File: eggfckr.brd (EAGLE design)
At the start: 100 x 80 mm, 7 parts, among them IC1 LM555N

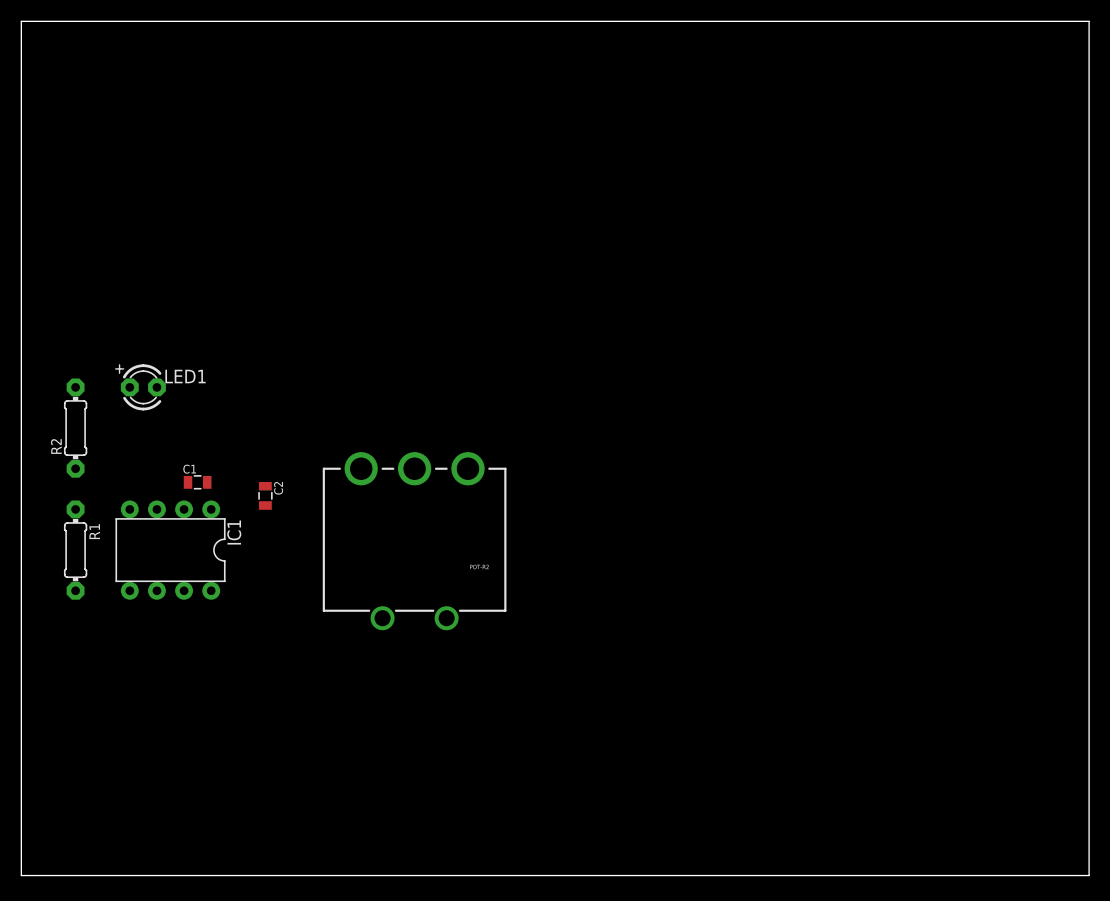
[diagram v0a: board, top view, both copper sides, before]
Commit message: attiny85 version
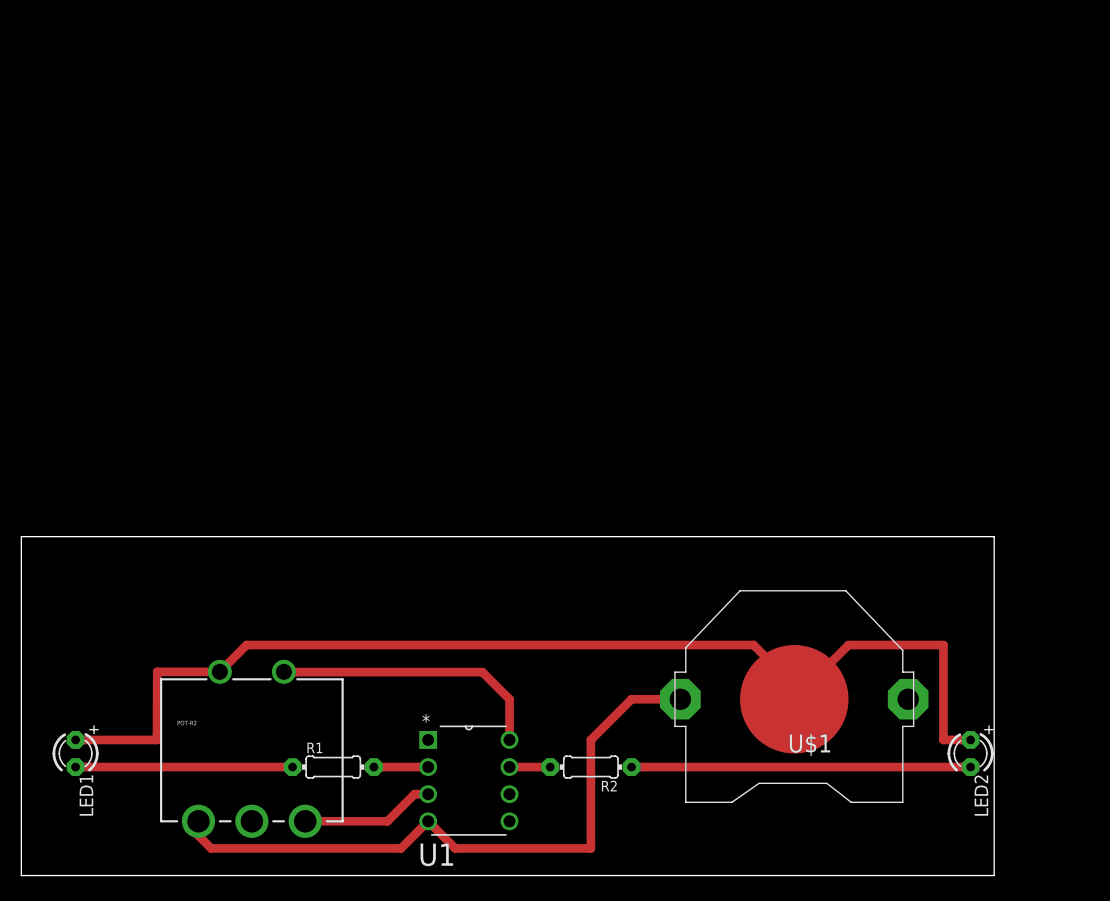
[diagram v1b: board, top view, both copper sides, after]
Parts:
- removed C1: 47uF, ATtami:0805
- removed C2: 10nF, ATtami:0805
- removed IC1: LM555N, adafruit:DIL08-ROUND
- added LED2: (no value), adafruit:LED3MM
- added U$1: (no value), adafruit:CR2032-THRU
- added U1: ATTINY85-20PU, Atmel_By_element14_Batch_1-00:DIP254P762X533-8
- moved R2 57.8 mm to (53.3, 10.2), turned to 180 degrees
- moved POT-R2 36.4 mm to (21.6, 5.08), turned to 0 degrees
- moved LED1 34.9 mm to (5.08, 11.4), turned to 270 degrees
- moved R1 31.5 mm to (29.2, 10.2), turned to 0 degrees
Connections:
- removed net N$5: IC1.8, POT-R2.S2
- removed net OUTPUT: IC1.3, LED1.K
- new net N$7: LED2.K, R2.1
- net GND: now also POT-R2.E@1, U$1.+2, U1.4; no longer C1.2, C2.1, IC1.1
- net N$1: now also R2.2, U1.7; no longer C2.2, IC1.5
- net N$2: now also POT-R2.E@2, U1.3; no longer C1.1, IC1.2, IC1.6, POT-R2.E@1
- net N$3: now also POT-R2.S2, U1.8; no longer POT-R2.S1
- net N$4: now also U1.2; no longer IC1.7, POT-R2.E@2
- net N$6: now also LED1.K, R1.1; no longer LED1.A, R2.2
- net VCC: now also LED1.A, LED2.A, POT-R2.S1, U$1.-; no longer IC1.4, R1.1, R2.1
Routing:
- net VCC: track 0.00 -> 108.1 mm
- net GND: track 0.00 -> 60.8 mm
- net N$7: track 0.00 -> 31.8 mm
- net N$3: track 0.00 -> 26.0 mm
- net N$6: track 0.00 -> 20.3 mm
- net N$2: track 0.00 -> 12.6 mm
- net N$4: track 0.00 -> 5.08 mm
- net N$1: track 0.00 -> 3.81 mm
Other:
- board size 100 x 80 mm -> 91.1 x 31.7 mm
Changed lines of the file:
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@@
 <board>
 <plain>
-<wire x1="0" y1="0" x2="100" y2="0" width="0" layer="20"/>
-<wire x1="100" y1="0" x2="100" y2="80" width="0" layer="20"/>
-<wire x1="100" y1="80" x2="0" y2="80" width="0" layer="20"/>
-<wire x1="0" y1="80" x2="0" y2="0" width="0" layer="20"/>
+<wire x1="0" y1="0" x2="91.11" y2="0" width="0" layer="20"/>
+<wire x1="91.11" y1="0" x2="91.11" y2="31.74" width="0" layer="20"/>
+<wire x1="91.11" y1="31.74" x2="0" y2="31.74" width="0" layer="20"/>
+<wire x1="0" y1="31.74" x2="0" y2="0" width="0" layer="20"/>
 </plain>
 <attributes>
@@
 </autorouter>
 <elements>
-<element name="C1" library="ATtami" package="0805" value="47uF" x="16.51" y="36.83"/>
-<element name="C2" library="ATtami" package="0805" value="10nF" x="22.86" y="35.56" rot="R270"/>
-<element name="IC1" library="adafruit" package="DIL08-ROUND" value="LM555N" x="13.97" y="30.48" rot="R180"/>
-<element name="POT-R2" library="SparkFun-Electromechanical" package="POT_PTH" value="5K" x="36.83" y="38.1" rot="R180"/>
-<element name="R1" library="adafruit" package="0204/7" value="" x="5.08" y="30.48" rot="R270"/>
-<element name="LED1" library="adafruit" package="LED3MM" value="" x="11.43" y="45.72"/>
-<element name="R2" library="adafruit" package="0204/7" value="" x="5.08" y="41.91" rot="R90"/>
+<element name="POT-R2" library="SparkFun-Electromechanical" package="POT_PTH" value="5K" x="21.59" y="5.08"/>
+<element name="LED1" library="adafruit" package="LED3MM" value="" x="5.08" y="11.43" rot="R270"/>
+<element name="R2" library="adafruit" package="0204/7" value="" x="53.34" y="10.16" rot="R180"/>
+<element name="U1" library="Atmel_By_element14_Batch_1-00" package="DIP254P762X533-8" value="ATTINY85-20PU" x="45.72" y="5.08">
+<attribute name="PACKAGE" value="PDIP-8" x="45.72" y="5.08" size="1.778" layer="27" display="off"/>
+<attribute name="OC_NEWARK" value="58M3796" x="45.72" y="5.08" size="1.778" layer="27" display="off"/>
+<attribute name="MPN" value="ATTINY85-20PU" x="45.72" y="5.08" size="1.778" layer="27" display="off"/>
+<attribute name="SUPPLIER" value="Atmel" x="45.72" y="5.08" size="1.778" layer="27" display="off"/>
+<attribute name="OC_FARNELL" value="1455162" x="45.72" y="5.08" size="1.778" layer="27" display="off"/>
+</element>
+<element name="R1" library="adafruit" package="0204/7" value="" x="29.21" y="10.16"/>
+<element name="LED2" library="adafruit" package="LED3MM" value="" x="88.9" y="11.43" rot="R270"/>
+<element name="U$1" library="adafruit" package="CR2032-THRU" value="" x="72.39" y="16.51" rot="R180"/>
 </elements>
 <signals>
 <signal name="N$1">
-<contactref element="C2" pad="2"/>
-<contactref element="IC1" pad="5"/>
-<wire x1="10.16" y1="26.67" x2="22.86" y2="34.66" width="0" layer="19" extent="1-1"/>
+<contactref element="U1" pad="7"/>
+<contactref element="R2" pad="2"/>
+<wire x1="45.72" y1="10.16" x2="49.53" y2="10.16" width="0.8128" layer="1"/>
+</signal>
+<signal name="N$6">
+<contactref element="R1" pad="1"/>
+<contactref element="LED1" pad="K"/>
+<wire x1="5.08" y1="10.16" x2="25.4" y2="10.16" width="0.8128" layer="1"/>
+</signal>
+<signal name="N$7">
+<contactref element="R2" pad="1"/>
+<contactref element="LED2" pad="K"/>
+<wire x1="57.15" y1="10.16" x2="88.9" y2="10.16" width="0.8128" layer="1"/>
 </signal>
 <signal name="GND">
-<contactref element="C2" pad="1"/>
-<contactref element="IC1" pad="1"/>
-<contactref element="C1" pad="2"/>
-<wire x1="17.41" y1="36.83" x2="22.86" y2="36.46" width="0" layer="19" extent="1-1"/>
-<wire x1="17.78" y1="34.29" x2="17.41" y2="36.83" width="0" layer="19" extent="1-1"/>
+<contactref element="U1" pad="4"/>
+<contactref element="POT-R2" pad="E@1"/>
+<contactref element="U$1" pad="+2"/>
+<wire x1="16.59" y1="5.08" x2="16.59" y2="3.73" width="0.8128" layer="1"/>
+<wire x1="16.59" y1="3.73" x2="17.78" y2="2.54" width="0.8128" layer="1"/>
+<wire x1="17.78" y1="2.54" x2="35.56" y2="2.54" width="0.8128" layer="1"/>
+<wire x1="35.56" y1="2.54" x2="38.1" y2="5.08" width="0.8128" layer="1"/>
+<wire x1="61.722" y1="16.51" x2="57.15" y2="16.51" width="0.8128" layer="1"/>
+<wire x1="57.15" y1="16.51" x2="53.34" y2="12.7" width="0.8128" layer="1"/>
+<wire x1="53.34" y1="12.7" x2="53.34" y2="2.54" width="0.8128" layer="1"/>
+<wire x1="53.34" y1="2.54" x2="40.64" y2="2.54" width="0.8128" layer="1"/>
+<wire x1="40.64" y1="2.54" x2="38.1" y2="5.08" width="0.8128" layer="1"/>
 </signal>
 <signal name="VCC">
-<contactref element="R1" pad="1"/>
-<contactref element="IC1" pad="4"/>
-<contactref element="R2" pad="1"/>
-<wire x1="5.08" y1="34.29" x2="10.16" y2="34.29" width="0" layer="19" extent="1-1"/>
-<wire x1="5.08" y1="38.1" x2="5.08" y2="34.29" width="0" layer="19" extent="1-1"/>
+<contactref element="POT-R2" pad="S1"/>
+<contactref element="LED2" pad="A"/>
+<contactref element="LED1" pad="A"/>
+<contactref element="U$1" pad="-"/>
+<wire x1="88.9" y1="12.7" x2="86.36" y2="12.7" width="0.8128" layer="1"/>
+<wire x1="86.36" y1="12.7" x2="86.36" y2="21.59" width="0.8128" layer="1"/>
+<wire x1="86.36" y1="21.59" x2="77.47" y2="21.59" width="0.8128" layer="1"/>
+<wire x1="77.47" y1="21.59" x2="72.39" y2="16.51" width="0.8128" layer="1"/>
+<wire x1="72.39" y1="16.51" x2="71.12" y2="15.24" width="0.8128" layer="1"/>
+<wire x1="71.12" y1="15.24" x2="71.12" y2="16.51" width="0.8128" layer="1"/>
+<wire x1="72.39" y1="16.51" x2="72.39" y2="17.78" width="0.8128" layer="1"/>
+<wire x1="72.39" y1="17.78" x2="68.58" y2="21.59" width="0.8128" layer="1"/>
+<wire x1="68.58" y1="21.59" x2="21.1" y2="21.59" width="0.8128" layer="1"/>
+<wire x1="21.1" y1="21.59" x2="18.59" y2="19.08" width="0.8128" layer="1"/>
+<wire x1="18.59" y1="19.08" x2="12.73" y2="19.08" width="0.8128" layer="1"/>
+<wire x1="12.73" y1="19.08" x2="12.7" y2="12.7" width="0.8128" layer="1"/>
+<wire x1="12.7" y1="12.7" x2="5.08" y2="12.7" width="0.8128" layer="1"/>
+</signal>
+<signal name="N$3">
+<contactref element="U1" pad="8"/>
+<contactref element="POT-R2" pad="S2"/>
+<wire x1="45.72" y1="12.7" x2="45.72" y2="16.51" width="0.8128" layer="1"/>
+<wire x1="45.72" y1="16.51" x2="43.18" y2="19.05" width="0.8128" layer="1"/>
+<wire x1="43.18" y1="19.05" x2="24.62" y2="19.05" width="0.8128" layer="1"/>
+<wire x1="24.62" y1="19.05" x2="24.59" y2="19.08" width="0.8128" layer="1"/>
 </signal>
 <signal name="N$2">
-<contactref element="IC1" pad="6"/>
-<contactref element="IC1" pad="2"/>
-<contactref element="C1" pad="1"/>
-<contactref element="POT-R2" pad="E@1"/>
-<wire x1="15.61" y1="36.83" x2="41.83" y2="38.1" width="0" layer="19" extent="1-1"/>
-<wire x1="15.24" y1="34.29" x2="15.61" y2="36.83" width="0" layer="19" extent="1-1"/>
-<wire x1="12.7" y1="26.67" x2="15.24" y2="34.29" width="0" layer="19" extent="1-1"/>
-</signal>
-<signal name="OUTPUT">
-<contactref element="IC1" pad="3"/>
-<contactref element="LED1" pad="K"/>
-<wire x1="12.7" y1="34.29" x2="12.7" y2="45.72" width="0" layer="19" extent="1-1"/>
+<contactref element="U1" pad="3"/>
+<contactref element="POT-R2" pad="E@2"/>
+<wire x1="26.59" y1="5.08" x2="34.29" y2="5.08" width="0.8128" layer="1"/>
+<wire x1="34.29" y1="5.08" x2="36.83" y2="7.62" width="0.8128" layer="1"/>
+<wire x1="36.83" y1="7.62" x2="38.1" y2="7.62" width="0.8128" layer="1"/>
 </signal>
 <signal name="N$4">
-<contactref element="IC1" pad="7"/>
-<contactref element="POT-R2" pad="E@2"/>
+<contactref element="U1" pad="2"/>
 <contactref element="R1" pad="2"/>
-<wire x1="15.24" y1="26.67" x2="31.83" y2="38.1" width="0" layer="19" extent="1-1"/>
-<wire x1="5.08" y1="26.67" x2="15.24" y2="26.67" width="0" layer="19" extent="1-1"/>
-</signal>
-<signal name="N$5">
-<contactref element="IC1" pad="8"/>
-<contactref element="POT-R2" pad="S2"/>
-<wire x1="17.78" y1="26.67" x2="33.83" y2="24.1" width="0" layer="19" extent="1-1"/>
-</signal>
-<signal name="N$3">
-<contactref element="POT-R2" pad="S1"/>
-</signal>
-<signal name="N$6">
-<contactref element="LED1" pad="A"/>
-<contactref element="R2" pad="2"/>
-<wire x1="5.08" y1="45.72" x2="10.16" y2="45.72" width="0" layer="19" extent="1-1"/>
+<wire x1="33.02" y1="10.16" x2="38.1" y2="10.16" width="0.8128" layer="1"/>
 </signal>
 </signals>
